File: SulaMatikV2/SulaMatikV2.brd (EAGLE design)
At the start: 66 x 61 mm, 39 parts, among them IC1 REG1117, Q1 2N3904, Q2 2N5551, Q3 2N5551

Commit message: v2
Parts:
- removed GPI3, GPI4: SWITCH-MOMENTARY-2PTH, SparkFun-Electromechanical:TACTILE-PTH
- removed R19: 10K, pot:CA6V
- removed R4, R5: 10k, SparkFun-Passives:0805
- removed SV2: (no value), con-lsta:FE08
- added BT: (no value), con-lstb:MA04-1
- added LED2: (no value), led:CHIP-LED0805
- added RTC: (no value), con-lsta:FE05-1
- moved R18 30.9 mm to (35.6, 12.7)
- moved R16 25.9 mm to (30.5, 15.2)
- moved R17 25.9 mm to (30.5, 10.2)
- moved D2 16.3 mm to (20.3, 55.9), turned to 0 degrees
- moved LED1 15.5 mm to (30.5, 58.4)
- moved Q3 15.5 mm to (25.4, 20.3)
- moved Q2 13.0 mm to (22.9, 7.62)
- moved R12 13.0 mm to (33.0, 53.3)
- moved JP7 12.7 mm to (36.8, 29.2)
- moved LIGHT 12.7 mm to (53.3, 20.3)
- moved MS 12.7 mm to (53.3, 10.2)
- moved PS 12.7 mm to (48.3, 5.08)
- moved PUMP 12.7 mm to (53.3, 15.2)
- moved R7 12.7 mm to (43.2, 43.2)
- moved SV1 12.7 mm to (45.7, 25.4)
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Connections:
- new net N$12: RTC.2
- new net N$14: RTC.1
- new net N$15: BT.4
- new net N$16: BT.3
- new net N$21: BT.1
- new net N$22: LED2.A, R1.1
- new net N$8: RTC.4
- new net SGND: D4.A, LED2.C, Q2.3, R16.2, R17.2, R18.2, R7.2
- net D4: no longer GPI3.3, R4.2
- net D5: no longer GPI4.3, R5.2
- net D6: no longer SV2.1
- net D7: no longer SV2.2
- net D8: no longer SV2.3
- net D9: no longer SV2.4
- net GND: no longer R16.2, R17.2, R18.2, R4.1, R5.1, R7.2
- net MOSI: no longer SV2.5
- net N$10: now also RTC.3; no longer D4.A, Q2.3, R1.1, SV2.8
- net N$17: now also BT.2; no longer MS.2, R19.E
- net N$3: now also RTC.5; no longer R1.2, SV2.7
- net VCC: now also MS.2, R1.2; no longer GPI3.1, GPI4.1, R19.S, SV2.6
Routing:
- net SGND: track 0.00 -> 132.0 mm
- net MOSI: track 90.5 -> 0.00 mm, vias 1 -> 0
- net D6: track 85.5 -> 0.00 mm
- net N$10: track 60.3 -> 0.00 mm
- net SCK: track 56.9 -> 0.00 mm
- net D8: track 55.8 -> 0.00 mm, vias 1 -> 0
- net D7: track 54.8 -> 0.00 mm, vias 1 -> 0
- net D5: track 53.9 -> 0.00 mm, vias 1 -> 0
- net VCC: track 241.1 -> 192.5 mm
- net D9: track 44.6 -> 0.00 mm, vias 1 -> 0
- net D2: track 41.7 -> 0.00 mm
- net N$22: track 0.00 -> 41.2 mm
- net GND: track 226.2 -> 185.3 mm
- net A0: track 96.7 -> 61.9 mm
- net A2: track 81.9 -> 57.0 mm, vias 2 -> 1
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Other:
- board size 66 x 61 mm -> 53.3 x 63.5 mm

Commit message: v2
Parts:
- added R2: 1K, SparkFun-Passives:0805
- added R4: 2.2K, SparkFun-Passives:0805
- added R5, R6: 1.8K, SparkFun-Passives:0805
- added R8, R9: 3.3K, SparkFun-Passives:0805
- added SD: (no value), con-lsta:FE08-2
- moved JP2 18.5 mm to (31.8, 40.6)
- moved D1 3.59 mm to (25.4, 40.6)
- moved R14 2.54 mm to (33.0, 27.9)
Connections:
- removed net N$10: RTC.3
- removed net N$12: RTC.2
- removed net N$14: RTC.1
- removed net N$15: BT.4
- removed net N$16: BT.3
- removed net N$17: BT.2
- removed net N$21: BT.1
- removed net N$3: RTC.5
- removed net N$8: RTC.4
- new net N$29: SD.3, SD.4
- new net SDCS: R6.2, R8.1, SD.7, SD.8
- new net SDMO: R5.2, R9.1, SD.10, SD.9
- new net SDSCK: R2.2, R4.1, SD.11, SD.12
- net D2: now also BT.1
- net D3: now also BT.2; no longer R14.2
- net D4: now also R6.1
- net D5: now also R14.2
- net D6: now also RTC.3
- net D7: now also RTC.2
- net D8: now also RTC.1
- net D9: now also R11.2
- net GND: now also BT.3, R4.2, R8.2, R9.2, RTC.4, SD.1, SD.15, SD.16, SD.2
- net MISO: now also SD.13, SD.14; no longer R11.2
- net MOSI: now also R5.1
- net SCK: now also R2.1
- net VCC: now also BT.4, RTC.5, SD.5, SD.6
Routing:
- net GND: track 185.3 -> 275.0 mm, vias 1 -> 5
- net SCK: track 0.00 -> 78.7 mm, vias 0 -> 1
- net D2: track 0.00 -> 56.9 mm, vias 0 -> 1
- net SDMO: track 0.00 -> 51.5 mm, vias 0 -> 1
- net A1: track 99.8 -> 49.0 mm, vias 0 -> 2
- net D8: track 0.00 -> 50.0 mm
- net D7: track 0.00 -> 47.9 mm
- net SDSCK: track 0.00 -> 47.3 mm
- net SGND: track 132.0 -> 85.1 mm
- net D6: track 0.00 -> 45.9 mm, vias 0 -> 1
- net SDCS: track 0.00 -> 43.5 mm, vias 0 -> 1
- net D4: track 0.00 -> 41.5 mm, vias 0 -> 1
- net MOSI: track 0.00 -> 40.7 mm, vias 0 -> 1
- net D3: track 20.0 -> 52.6 mm
- net MISO: track 27.3 -> 56.2 mm, vias 1 -> 0
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
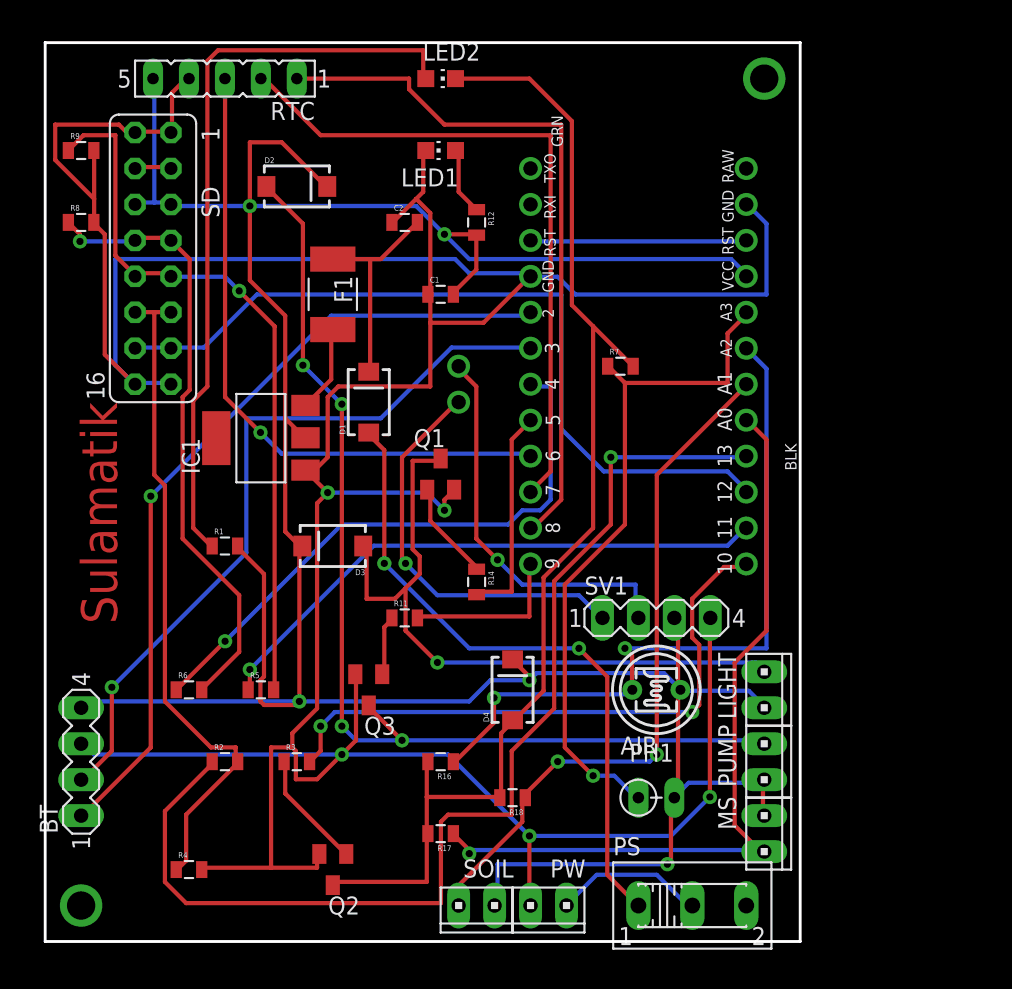
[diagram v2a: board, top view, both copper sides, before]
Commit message: battry buzzer eksik
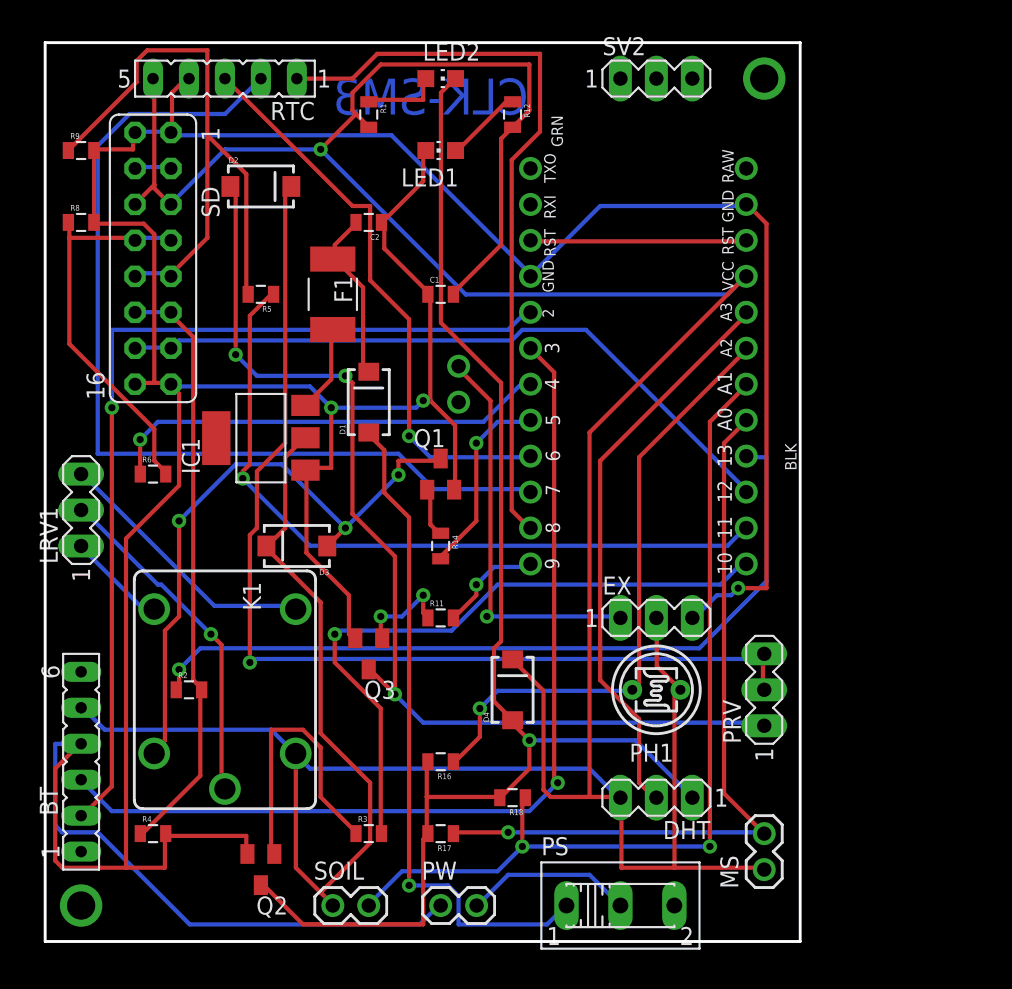
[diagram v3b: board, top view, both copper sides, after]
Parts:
- removed AIR: THERMISTOR-2,5, varistor:RS-2,5
- removed LIGHT, PUMP: (no value), con-amp:10X02MTA
- removed R7: 10K, SparkFun-Passives:0805
- removed SV1: (no value), con-lstb:MA04-1
- added DHT, EX, LRV1, PRV, SV2: (no value), con-lstb:MA03-1
- added K1: CQ1-12V, relay:CQ1
- BT: device con-lstb:MA04-1 -> con-lsta:FE06
- F1: value 1.5A -> 1A
- MS, PW, SOIL: device con-amp:10X02MTA -> SparkFun:1X02
- moved R1 32.1 mm to (25.4, 61.0), turned to 270 degrees
- moved R5 27.9 mm to (17.8, 48.3), turned to 180 degrees
- moved R6 15.5 mm to (10.2, 35.6)
- moved SOIL 10.2 mm to (22.9, 5.08), turned to 0 degrees
- moved R12 8.03 mm to (35.6, 61.0)
- moved PW 7.62 mm to (30.5, 5.08), turned to 0 degrees
- moved R3 7.18 mm to (25.4, 10.2)
- moved R2 5.68 mm to (12.7, 20.3)
- moved PS 5.08 mm to (43.2, 5.08)
- moved Q2 5.08 mm to (17.8, 7.62)
- moved R14 3.59 mm to (30.5, 30.5)
- moved R4 3.59 mm to (10.2, 10.2)
- moved C2 2.54 mm to (25.4, 53.3), turned to 180 degrees
- moved MS 2.54 mm to (53.3, 7.62), turned to 90 degrees
- moved D2 2.54 mm to (17.8, 55.9)
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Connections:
- new net N$10: K1.C, LRV1.2
- new net N$12: K1.NC, LRV1.1
- new net N$3: D2.C, PRV.2, PRV.3
- new net N$8: K1.NO, LRV1.3
- net A0: now also MS.2; no longer MS.1
- net A1: now also SOIL.2; no longer SOIL.1
- net A3: now also DHT.2; no longer AIR.1, R7.1
- net A4: no longer SV1.1
- net A5: now also EX.1; no longer SV1.2
- net D2: now also BT.2; no longer BT.1
- net D3: now also BT.3; no longer BT.2
- net GND: now also BT.4, EX.3; no longer BT.3, SV1.4
- net N$19: now also K1.1; no longer LIGHT.2
- net N$5: now also PRV.1; no longer PUMP.2
- net SGND: now also DHT.1; no longer R7.2
- net VCC: now also BT.5, DHT.3, EX.2, K1.2, MS.1, SOIL.1; no longer AIR.2, BT.4, D2.C, LIGHT.1, MS.2, PUMP.1, SOIL.2, SV1.3
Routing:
- net N$3: track 0.00 -> 74.1 mm, vias 0 -> 1
- net VCC: track 221.2 -> 277.8 mm, vias 5 -> 1
- net N$22: track 53.0 -> 5.60 mm
- net A4: track 28.9 -> 0.00 mm, vias 1 -> 0
- net N$10: track 0.00 -> 24.2 mm, vias 0 -> 1
- net SCK: track 78.7 -> 55.8 mm
- net N$8: track 0.00 -> 19.1 mm
- net D7: track 47.9 -> 67.0 mm
- net SDCS: track 43.5 -> 28.1 mm, vias 1 -> 0
- net D3: track 52.6 -> 66.9 mm
- net A1: track 49.0 -> 63.1 mm
- net SGND: track 85.1 -> 97.8 mm, vias 0 -> 1
- net N$7: track 8.33 -> 20.1 mm
- net MOSI: track 40.7 -> 52.1 mm
- net D4: track 41.5 -> 31.7 mm
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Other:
- board text added: "CLK-SM3"
- board text removed: "Sulamatik"

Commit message: tamam
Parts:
- removed SV2: (no value), con-lstb:MA03-1
- added R10: 14K, SparkFun-Passives:0805
- added R7: 20K, SparkFun-Passives:0805
- moved R4 33.4 mm to (5.08, 43.2), flipped to the bottom, turned to 180 degrees
- moved R2 29.0 mm to (5.08, 48.3), flipped to the bottom
- moved R6 20.5 mm to (20.3, 53.3), flipped to the bottom
- moved IC1 5.68 mm to (12.7, 35.6), flipped to the bottom, turned to 180 degrees
- moved R14 2.54 mm to (33.0, 30.5)
- moved Q2 2.54 mm to (15.2, 7.62), flipped to the bottom, turned to 270 degrees
- moved C1 2.54 mm to (30.5, 50.8)
- moved D1 2.54 mm to (25.4, 38.1)
- moved D3 2.54 mm to (22.9, 30.5), turned to 90 degrees
- moved LED1 2.54 mm to (30.5, 55.9)
- moved LED2 2.54 mm to (30.5, 61.0)
- moved R5 2.54 mm to (20.3, 48.3), flipped to the bottom, turned to 0 degrees
- flipped K1 to the bottom, turned to 90 degrees
- turned Q1 to 90 degrees
- turned R1 to 180 degrees
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- renumbered EX to BZZ
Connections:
- net A4: now also R10.2, R7.1
- net SGND: now also R10.1
- net VCC9V: now also R7.2
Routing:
- net GND: track 282.0 -> 233.2 mm, vias 3 -> 2
- net A4: track 0.00 -> 45.7 mm
- net SDSCK: track 42.1 -> 12.5 mm
- net VCC: track 277.8 -> 250.2 mm, vias 1 -> 3
- net VCC9V: track 12.3 -> 37.7 mm, vias 0 -> 2
- net SDMO: track 45.8 -> 24.6 mm
- net SGND: track 97.8 -> 117.3 mm
- net D7: track 67.0 -> 47.5 mm, vias 0 -> 1
- net SCK: track 55.8 -> 75.3 mm
- net N$19: track 43.6 -> 27.3 mm, vias 3 -> 2
- net SDCS: track 28.1 -> 14.7 mm
- net N$10: track 24.2 -> 12.5 mm, vias 1 -> 0
- net N$8: track 19.1 -> 30.5 mm, vias 0 -> 1
- net N$7: track 20.1 -> 8.92 mm
- net N$12: track 7.03 -> 18.0 mm
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
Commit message: almost v2
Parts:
- removed K1: CQ1-12V, relay:CQ1
- removed LRV1: (no value), con-lstb:MA03-1
- added LRV: (no value), SparkFun:1X02
- PRV: device con-lstb:MA03-1 -> con-lsta:FE05-1
- R10: value 14K -> 22K
- R7: value 20K -> 47K
- moved Q3 13.7 mm to (12.7, 17.8), flipped to the bottom, turned to 0 degrees
- moved D3 7.62 mm to (22.9, 22.9)
- moved R16 5.08 mm to (25.4, 15.2)
- moved D1 3.59 mm to (22.9, 35.6)
- moved IC1 3.59 mm to (10.2, 33.0)
- moved MS 2.54 mm to (53.3, 5.08)
- moved PRV 2.54 mm to (53.3, 17.8)
- moved Q1 2.54 mm to (30.5, 33.0)
- moved R11 2.54 mm to (30.5, 22.9)
- moved R14 2.54 mm to (33.0, 27.9)
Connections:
- removed net N$10: K1.C, LRV1.2
- removed net N$12: K1.NC, LRV1.1
- removed net N$8: K1.NO, LRV1.3
- net GND: now also PRV.1
- net N$19: now also LRV.1; no longer K1.1
- net N$3: now also PRV.4; no longer PRV.2
- net N$5: now also PRV.2; no longer PRV.1
- net VCC: now also LRV.2, PRV.5; no longer K1.2
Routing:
- net N$8: track 30.5 -> 0.00 mm, vias 1 -> 0
- net VCC: track 250.2 -> 275.7 mm, vias 3 -> 1
- net VCC9V: track 37.7 -> 58.7 mm, vias 2 -> 0
- net N$12: track 18.0 -> 0.00 mm
- net N$6: track 4.58 -> 18.5 mm, vias 0 -> 1
- net N$10: track 12.5 -> 0.00 mm
- net A4: track 45.7 -> 34.4 mm, vias 0 -> 1
- net N$19: track 27.3 -> 36.0 mm, vias 2 -> 1
- net GND: track 233.2 -> 241.9 mm, vias 2 -> 1
- net N$5: track 73.9 -> 79.4 mm, vias 2 -> 1
- net A5: track 30.6 -> 25.2 mm
- net A1: track 55.8 -> 50.9 mm
- net D2: track 65.7 -> 61.4 mm
- net N$1: track 14.0 -> 18.2 mm
- net A0: track 54.5 -> 57.9 mm, vias 1 -> 2
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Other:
- board text added: "CLK-SM2"
- board text removed: "CLK-SM3"

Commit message: sync
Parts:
- moved R2 13.7 mm to (17.8, 43.2)
- moved R9 10.2 mm to (5.08, 48.3)
- moved SOIL 10.2 mm to (12.7, 5.08)
- moved Q2 5.68 mm to (17.8, 12.7)
- moved PW 5.08 mm to (25.4, 5.08)
- moved PS 5.08 mm to (38.1, 5.08)
- moved R10 3.59 mm to (48.3, 55.9), turned to 180 degrees
- moved R7 3.59 mm to (43.2, 55.9)
- moved IC1 2.54 mm to (12.7, 33.0)
- moved Q3 2.54 mm to (12.7, 20.3)
- moved R5 2.54 mm to (17.8, 48.3)
- moved R6 2.54 mm to (17.8, 53.3)
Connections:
- net GND: now also R10.1
- net SGND: no longer R10.1
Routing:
- net SCK: track 77.7 -> 51.3 mm, vias 0 -> 2
- net VCC: track 275.7 -> 250.2 mm, vias 1 -> 3
- net A1: track 50.9 -> 71.6 mm
- net GND: track 241.9 -> 259.5 mm
- net N$13: track 49.0 -> 35.5 mm, vias 1 -> 0
- net SDMO: track 24.6 -> 12.3 mm
- net N$3: track 85.3 -> 73.5 mm, vias 0 -> 1
- net D3: track 65.3 -> 53.5 mm
- net D2: track 61.4 -> 72.6 mm
- net SDSCK: track 12.5 -> 20.3 mm
- net MISO: track 58.0 -> 51.2 mm, vias 1 -> 2
- net A3: track 37.5 -> 43.7 mm
- net VCC9V: track 58.7 -> 52.5 mm
- net N$7: track 8.92 -> 15.0 mm
- net MOSI: track 45.8 -> 51.8 mm
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
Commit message: sav
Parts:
- added PRV1: (no value), SparkFun-Connectors:1X03
- added PRVIN: (no value), SparkFun:1X02
- BZZ, DHT: device con-lstb:MA03-1 -> SparkFun-Connectors:1X03
- PRV: device con-lsta:FE05-1 -> SparkFun-Connectors:1X03
- PS: device switch:255SB -> SparkFun-Connectors:1X03
- moved R17 13.7 mm to (35.6, 22.9)
- moved R16 13.0 mm to (22.9, 27.9)
- moved D4 8.03 mm to (33.0, 12.7), turned to 180 degrees
- moved MS 5.08 mm to (48.3, 5.08), turned to 0 degrees
- moved IC1 5.08 mm to (12.7, 27.9)
- moved PW 5.08 mm to (30.5, 5.08)
- moved R18 5.08 mm to (35.6, 17.8)
- moved D3 5.08 mm to (22.9, 17.8), turned to 270 degrees
- moved LRV 2.54 mm to (5.08, 30.5), turned to 90 degrees
- moved BZZ 2.54 mm to (43.2, 25.4)
- moved DHT 2.54 mm to (43.2, 12.7), turned to 0 degrees
- moved PRV 2.54 mm to (53.3, 20.3)
- moved Q3 2.54 mm to (12.7, 17.8)
- moved R11 2.54 mm to (27.9, 22.9)
- turned D1 to 180 degrees
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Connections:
- net GND: now also PRV1.3
- net N$3: now also PRVIN.1; no longer PRV.4
- net VCC: now also PRV1.2, PRVIN.2; no longer PRV.5
- net VCC9V: now also PRV1.1
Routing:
- net VCC9V: track 52.5 -> 85.6 mm
- net N$3: track 73.5 -> 92.9 mm, vias 1 -> 0
- net VCC: track 250.2 -> 233.7 mm, vias 3 -> 2
- net A3: track 43.7 -> 58.9 mm, vias 1 -> 0
- net D2: track 72.6 -> 60.9 mm
- net N$19: track 36.2 -> 47.8 mm
- net A4: track 31.6 -> 42.9 mm, vias 2 -> 1
- net GND: track 259.5 -> 248.4 mm, vias 1 -> 2
- net A2: track 47.3 -> 56.8 mm
- net D3: track 53.5 -> 62.6 mm, vias 1 -> 0
- net N$5: track 83.6 -> 75.8 mm
- net MISO: track 51.2 -> 58.8 mm, vias 2 -> 1
- net N$7: track 15.0 -> 8.53 mm
- net MOSI: track 51.8 -> 46.1 mm, vias 0 -> 1
- net SCK: track 51.3 -> 46.4 mm, vias 2 -> 0
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
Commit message: ad
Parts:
- R1, R12: value 330 -> 220
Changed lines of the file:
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@@
 <element name="D1" library="SparkFun-DiscreteSemi" package="SMA-DIODE" value="" x="22.86" y="35.56" rot="R180"/>
 <element name="C2" library="SparkFun-Capacitors" package="0805" value="100uf" x="25.4" y="53.34" rot="R180"/>
-<element name="R12" library="SparkFun-Passives" package="0805" value="330" x="35.56" y="60.96"/>
+<element name="R12" library="SparkFun-Passives" package="0805" value="220" x="35.56" y="60.96"/>
 <element name="F1" library="_hhn_PtcFuses_Siba_r500_Ozan" package="1820" value="1A" x="22.86" y="48.26" rot="R270"/>
 <element name="IC1" library="burr-brown" package="SOT223" value="REG1117" x="12.7" y="27.94" rot="MR180">
@@
 </element>
 <element name="LED2" library="led" package="CHIP-LED0805" value="" x="30.48" y="60.96" rot="R270"/>
-<element name="R1" library="SparkFun-Passives" package="0805" value="330" x="25.4" y="60.96" rot="R180"/>
+<element name="R1" library="SparkFun-Passives" package="0805" value="220" x="25.4" y="60.96" rot="R180"/>
 <element name="SD" library="con-lsta" package="FE08-2" value="" x="10.16" y="50.8" rot="R270">
 <attribute name="OC_NEWARK" value="unknown" x="10.16" y="50.8" size="1.778" layer="27" rot="R270" display="off"/>
